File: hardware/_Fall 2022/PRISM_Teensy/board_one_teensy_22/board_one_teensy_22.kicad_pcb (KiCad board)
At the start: 2 copper layers, 0 parts

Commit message: Add GPS EAST
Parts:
- added C1: 0.1uf, Capacitor_SMD:C_0805_2012Metric_Pad1.18x1.45mm_HandSolder, F.Cu at (171.4, 62.9)
- added D1: LED, LED_SMD:LED_0805_2012Metric_Pad1.15x1.40mm_HandSolder, F.Cu at (145.7, 63.3)
- added D2: LED, LED_SMD:LED_0805_2012Metric_Pad1.15x1.40mm_HandSolder, F.Cu at (141.2, 63.3)
- added D3: LED, LED_SMD:LED_0805_2012Metric_Pad1.15x1.40mm_HandSolder, F.Cu at (136.8, 63.3)
- added J1: Conn_01x04, Connector_JST:JST_PH_S4B-PH-K_1x04_P2.00mm_Horizontal, F.Cu at (137.9, 63.5)
- added J2: Conn_01x07, Connector_JST:JST_PH_S7B-PH-K_1x07_P2.00mm_Horizontal, F.Cu at (123.8, 80.2)
- added R1: 150, Resistor_SMD:R_0805_2012Metric_Pad1.20x1.40mm_HandSolder, F.Cu at (145.7, 61.0)
- added R2: 150, Resistor_SMD:R_0805_2012Metric_Pad1.20x1.40mm_HandSolder, F.Cu at (141.2, 60.9)
- added R3: 150, Resistor_SMD:R_0805_2012Metric_Pad1.20x1.40mm_HandSolder, F.Cu at (136.8, 60.9)
- added R4: 100K, Resistor_SMD:R_0805_2012Metric_Pad1.20x1.40mm_HandSolder, F.Cu at (171.4, 72.3)
- added R5: 300K, Resistor_SMD:R_0805_2012Metric_Pad1.20x1.40mm_HandSolder, F.Cu at (171.4, 67.5)
- added U1: Teensy4.1, Teensy:Teensy41, F.Cu at (159.8, 92.6)
- added U2: BNO055_Breakout, Olin_Rocketry:BNO055, F.Cu at (134.6, 80.8)

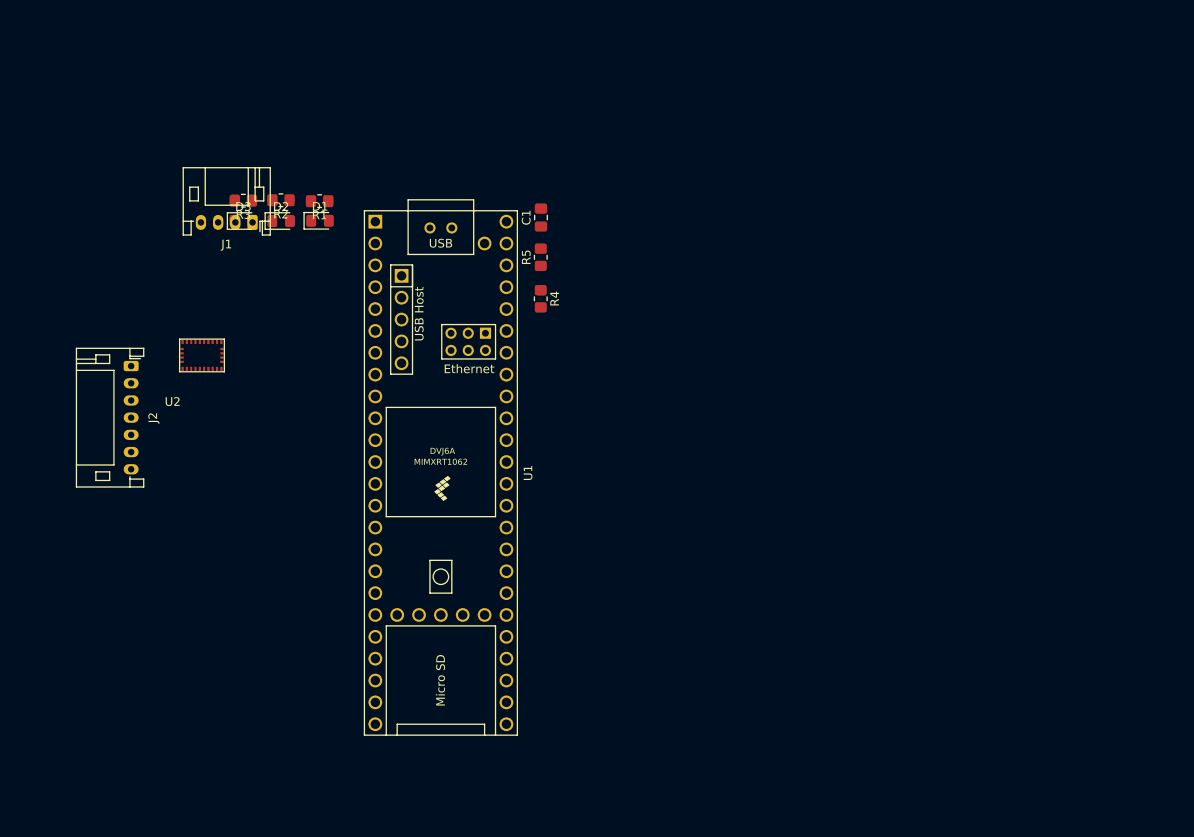
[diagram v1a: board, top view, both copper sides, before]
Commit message: reorganized PRISM FC
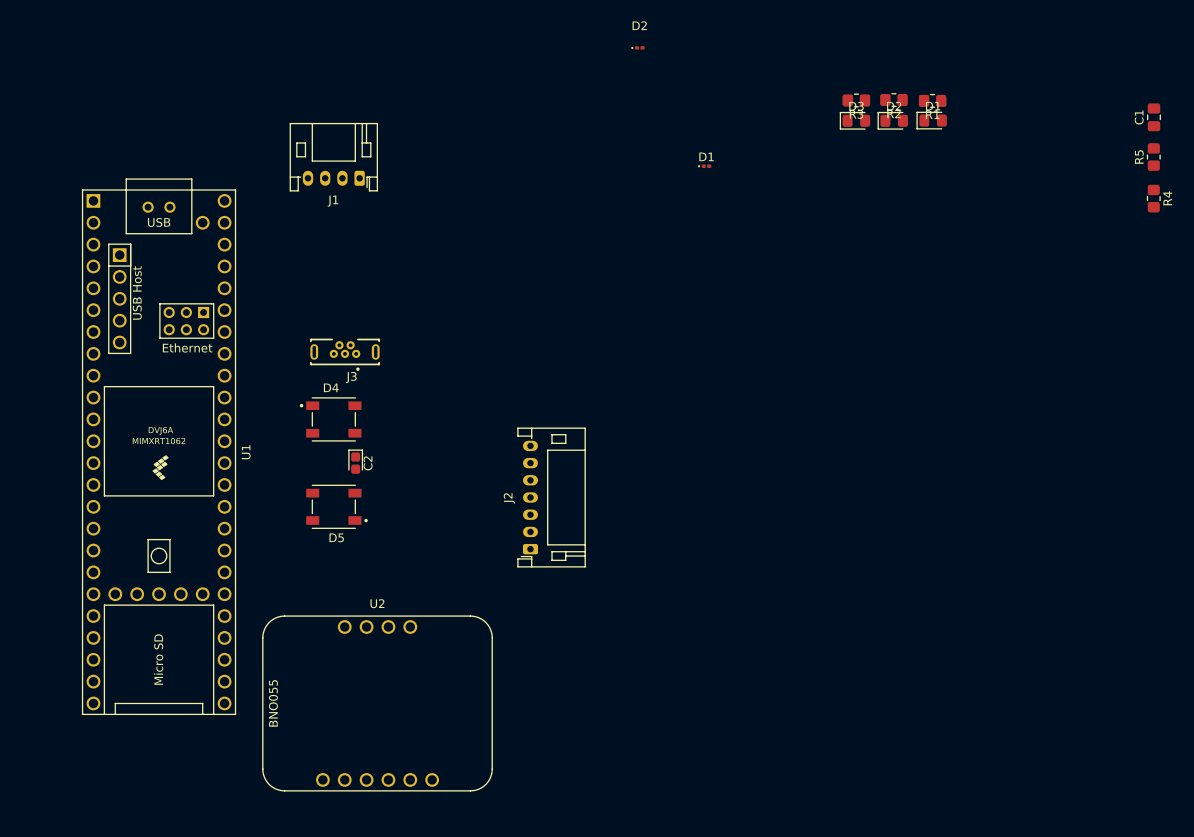
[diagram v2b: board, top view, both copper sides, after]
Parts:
- added C2: 0.1uf, Capacitor_Tantalum_SMD:CP_EIA-1608-08_AVX-J, F.Cu at (149.9, 91.4)
- added D1: DIODE, Diode_SMD:D_0201_0603Metric, F.Cu at (190.6, 56.9)
- added D2: DIODE, Diode_SMD:D_0201_0603Metric, F.Cu at (182.9, 43.2)
- added D4: Neopixel1, neopixel:LED_1655, F.Cu at (147.3, 86.4)
- added D5: Neopixel2, neopixel:LED_1655, F.Cu at (147.3, 96.5)
- added J3: USB_micro, USB:GCT_USB3131-30-0230-A_REVB, F.Cu at (148.6, 78.5)
- J1: value Conn_01x04 -> EAST
- J2: value Conn_01x07 -> CORE_IO
- U2: footprint Olin_Rocketry:BNO055 -> Sensors:BNO055_Breakout
- moved D1 72.2 mm to (217.0, 51.6)
- moved D3 72.2 mm to (208.1, 51.6)
- moved R3 72.2 mm to (208.1, 49.3)
- moved R4 72.2 mm to (242.6, 60.7)
- moved R5 72.2 mm to (242.6, 55.9)
- moved C1 72.2 mm to (242.7, 51.2)
- moved D2 72.2 mm to (212.5, 51.6)
- moved R1 72.2 mm to (216.9, 49.3)
- moved R2 72.2 mm to (212.4, 49.2)
- moved J2 51.1 mm to (170.2, 101.4), turned to 90 degrees
- moved U2 42.5 mm to (152.4, 119.4), turned to 0 degrees
- moved U1 32.9 mm to (127.0, 90.2)
- moved J1 13.5 mm to (150.3, 58.3)
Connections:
- R4 pad 1: /V_BATT -> /V_IN
- U1 pad 23: unconnected-(U1-Pad23) -> /NEOPIXEL
- U1 pad 48: /V_BATT -> /V_IN
- U1 pad 6: /LED 0 -> unconnected-(U1-Pad6)
- U1 pad 66: unconnected-(U1-Pad66) -> Net-(U1-Pad66)
- U1 pad 67: unconnected-(U1-Pad67) -> Net-(U1-Pad67)
- U1 pad 7: /LED 1 -> unconnected-(U1-Pad7)
- U1 pad 8: /LED 2 -> unconnected-(U1-Pad8)

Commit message: Add altimeter to footprint
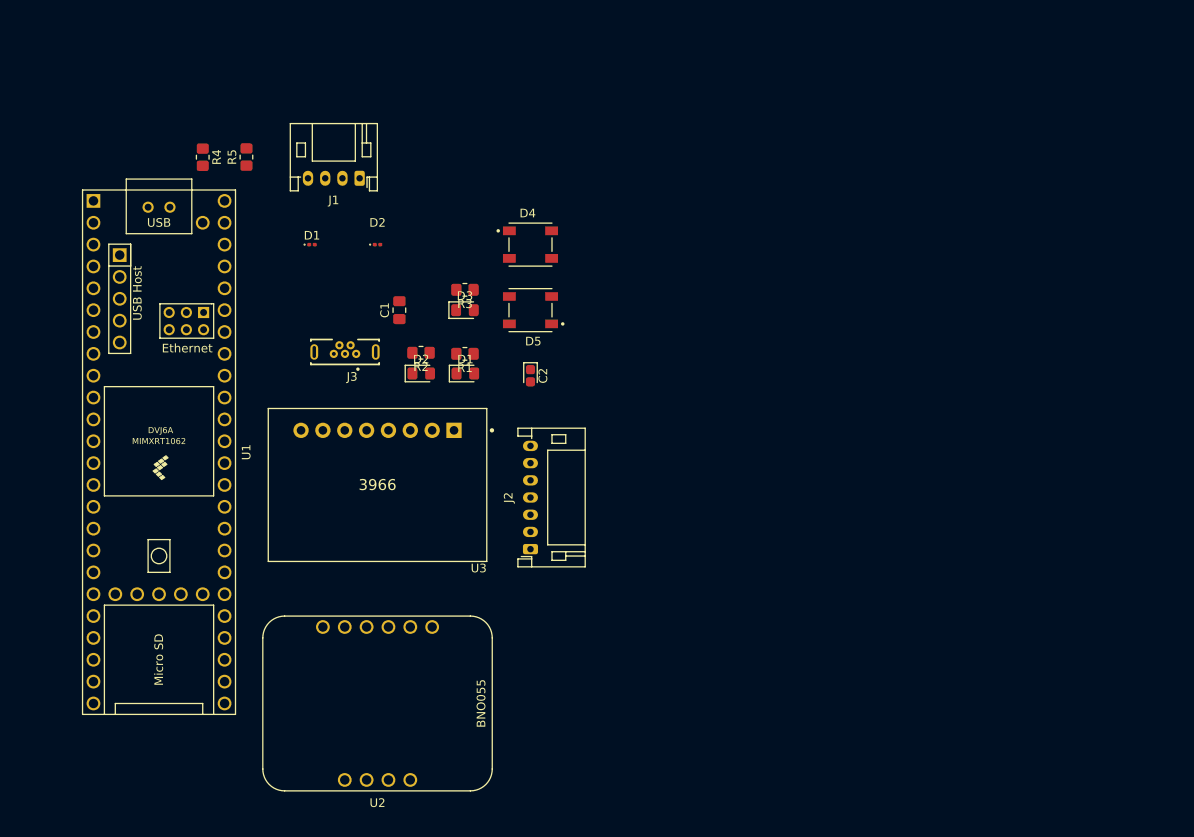
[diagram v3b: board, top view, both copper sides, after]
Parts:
- added U3: 3966, BMP388:Adafruit_Industries-3966-MFG, F.Cu at (152.4, 94.0)
- moved R4 110.7 mm to (132.1, 55.9)
- moved R5 105.5 mm to (137.2, 55.9)
- moved C1 90.5 mm to (154.9, 73.7)
- moved D2 62.3 mm to (157.5, 81.0)
- moved R2 62.3 mm to (157.5, 78.6)
- moved D1 61.8 mm to (162.6, 81.0)
- moved R1 61.8 mm to (162.6, 78.7)
- moved D3 50.5 mm to (162.6, 73.7)
- moved R3 50.5 mm to (162.6, 71.3)
- moved D1 46.8 mm to (144.8, 66.0)
- moved D2 38.1 mm to (152.4, 66.0)
- moved D5 32.3 mm to (170.2, 73.7)
- moved D4 30.6 mm to (170.2, 66.0)
- moved C2 22.7 mm to (170.2, 81.3)
- turned U2 to 180 degrees
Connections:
- J2 pad 1: GND -> /ARM
- J2 pad 2: /V_BATT -> /CONT 2
- J2 pad 3: /PYRO 1 -> /CONT 1
- J2 pad 5: /CONT 1 -> /PYRO 1
- J2 pad 6: /CONT 2 -> /VBAT
- J2 pad 7: /ARM -> GND

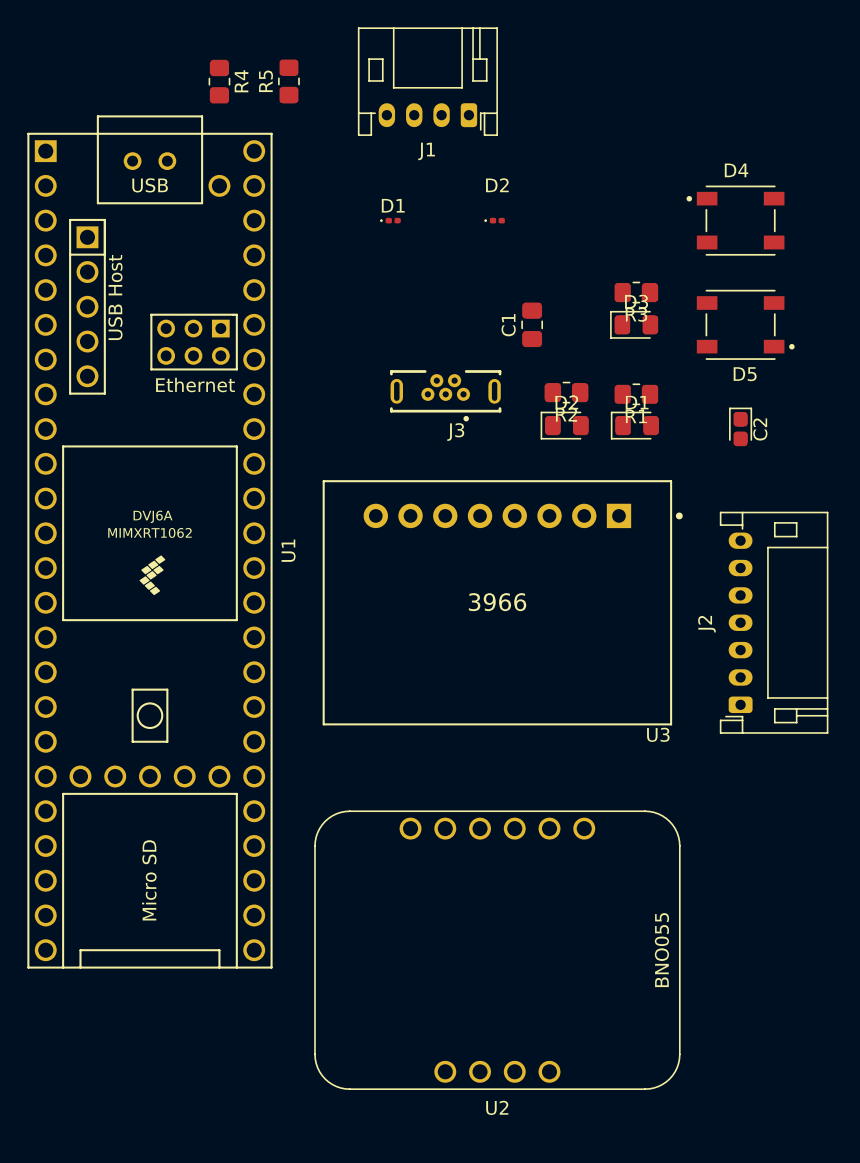
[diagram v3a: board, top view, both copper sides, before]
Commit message: Edit footprint layout and resistor sizes
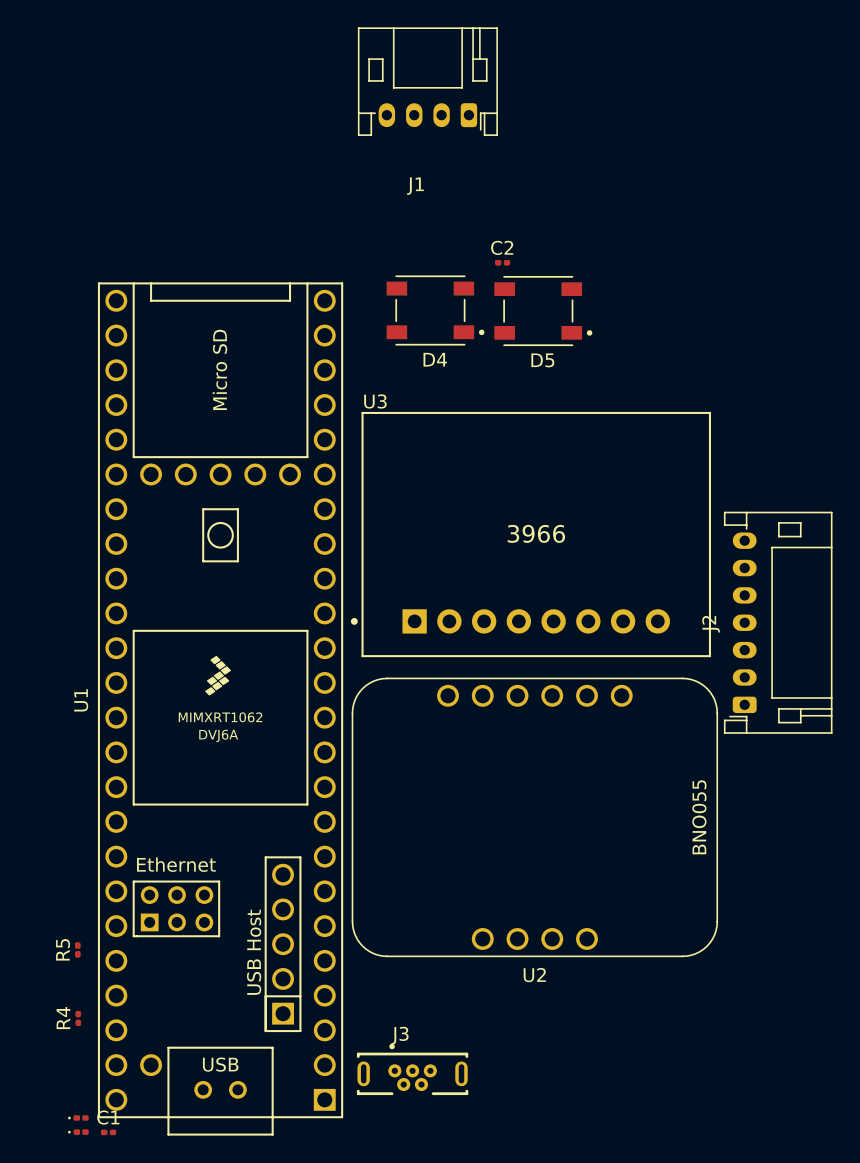
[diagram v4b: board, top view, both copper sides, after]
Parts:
- removed the D1 at (162.6, 81.0)
- removed the D2 at (157.5, 81.0)
- removed D3: LED, LED_SMD:LED_0805_2012Metric_Pad1.15x1.40mm_HandSolder
- removed R1, R2, R3: 150, Resistor_SMD:R_0805_2012Metric_Pad1.20x1.40mm_HandSolder
- C1: footprint Capacitor_SMD:C_0805_2012Metric_Pad1.18x1.45mm_HandSolder -> Capacitor_SMD:C_0201_0603Metric
- C2: footprint Capacitor_Tantalum_SMD:CP_EIA-1608-08_AVX-J -> Capacitor_SMD:C_0201_0603Metric
- R4, R5: footprint Resistor_SMD:R_0805_2012Metric_Pad1.20x1.40mm_HandSolder -> Resistor_SMD:R_0201_0603Metric
- moved D2 72.3 mm to (122.0, 131.7)
- moved D1 70.4 mm to (122.0, 132.7)
- moved R4 69.3 mm to (121.8, 124.4), turned to 90 degrees
- moved C1 66.7 mm to (124.0, 132.7), turned to 0 degrees
- moved R5 65.3 mm to (121.7, 119.4)
- moved J3 50.0 mm to (146.2, 128.4), turned to 0 degrees
- moved D4 23.6 mm to (147.5, 72.6), turned to 180 degrees
- moved C2 21.2 mm to (152.8, 69.1), turned to 0 degrees
- moved D5 14.8 mm to (155.4, 72.7)
- moved U1 12.1 mm to (132.2, 101.1), turned to 90 degrees
- moved U2 10.1 mm to (155.1, 109.7)
- moved U3 5.74 mm to (155.2, 89.0), turned to 0 degrees
- moved J2 0.30 mm to (170.5, 101.4)
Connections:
- R4 pad 1: /V_IN -> /VIN
- U1 pad 48: /V_IN -> /VIN

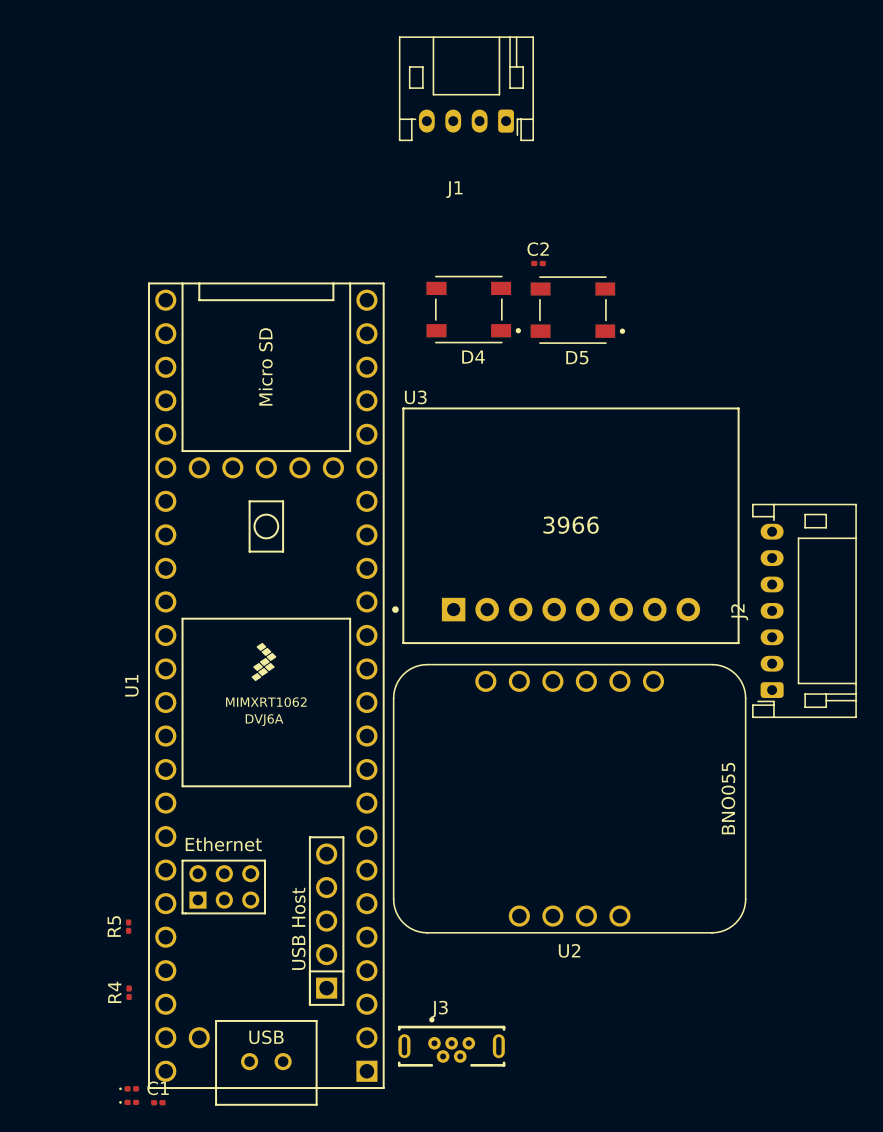
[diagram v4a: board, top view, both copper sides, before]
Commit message: Complete PRISM Teensy layout
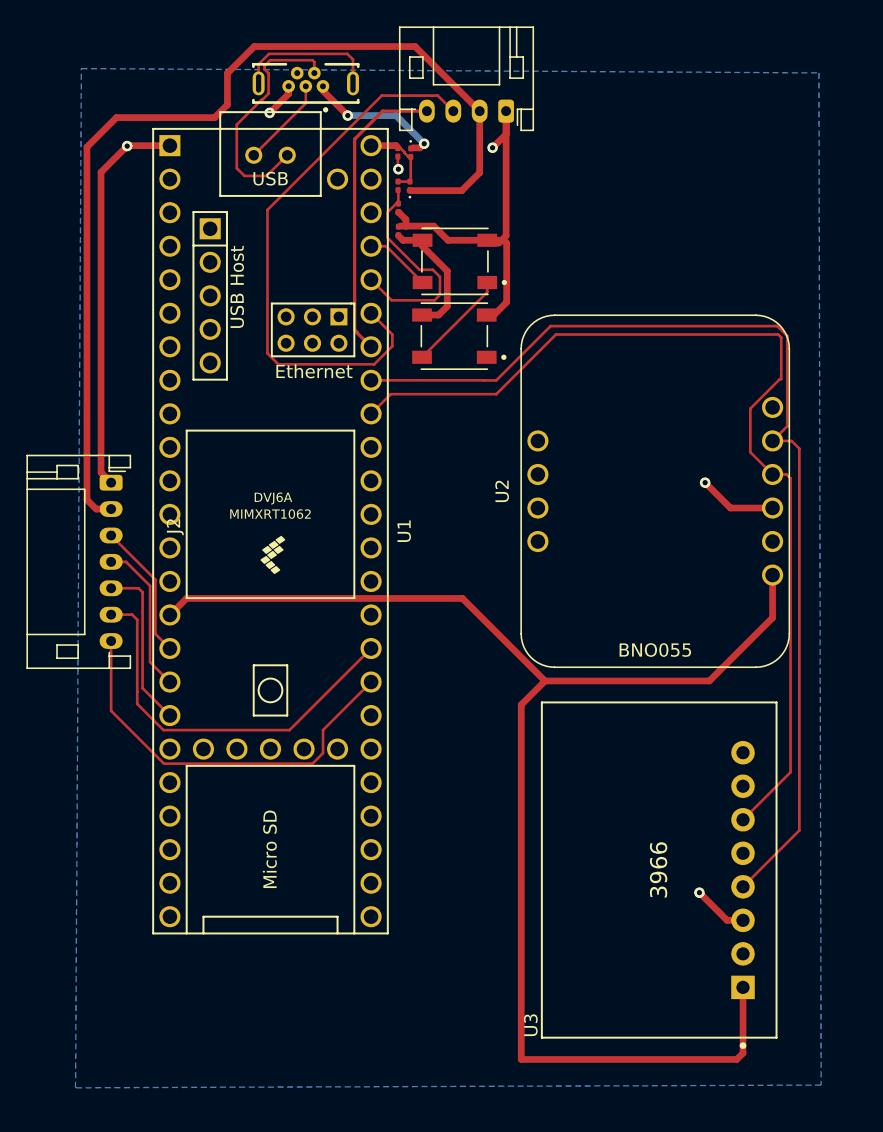
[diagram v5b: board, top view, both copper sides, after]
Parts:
- moved C1 74.3 mm to (142.1, 60.7), turned to -90 degrees
- moved D2 74.0 mm to (143.1, 60.7), turned to -90 degrees
- moved J3 73.8 mm to (135.2, 55.5), turned to 180 degrees
- moved D1 72.6 mm to (143.0, 63.2), turned to 90 degrees
- moved R4 64.4 mm to (142.1, 63.2), turned to -90 degrees
- moved R5 58.2 mm to (142.2, 64.9), turned to -90 degrees
- moved J2 52.5 mm to (120.4, 85.7), turned to -90 degrees
- moved U3 26.9 mm to (161.9, 115.1), turned to 90 degrees
- moved U2 24.2 mm to (161.6, 86.4), turned to 90 degrees
- moved U1 11.7 mm to (132.5, 89.4), turned to -90 degrees
- moved C2 10.9 mm to (142.2, 66.6), turned to -90 degrees
- moved D5 9.20 mm to (146.4, 74.6)
- moved D4 3.80 mm to (146.4, 69.0)
- moved J1 0.76 mm to (150.3, 57.6)
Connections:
- C1 pad 1: /V_BATT -> /VIN
- J1 pad 4: /RX 0  -> /RX 0
- J2 pad 1: /ARM -> GND
- J2 pad 2: /CONT 2 -> /V_BATT
- J2 pad 3: /CONT 1 -> /PYRO 1
- J2 pad 5: /PYRO 1 -> /ARM
- J2 pad 6: /VBAT -> /CONT 1
- J2 pad 7: GND -> /CONT 2
- J3 pad S1: Net-(J3-PadS1) -> unconnected-(J3-PadS1)
- J3 pad S2: Net-(J3-PadS1) -> unconnected-(J3-PadS1)
- U1 pad 10: /RX 0 -> unconnected-(U1-Pad10)
- U1 pad 23: /NEOPIXEL -> unconnected-(U1-Pad23)
- U1 pad 32: unconnected-(U1-Pad32) -> /CONT 2
- U1 pad 33: unconnected-(U1-Pad33) -> /CONT 1
- U1 pad 38: /CONT 2 -> unconnected-(U1-Pad38)
- U1 pad 39: /CONT 1 -> unconnected-(U1-Pad39)
- U1 pad 42: unconnected-(U1-Pad42) -> /RX 0
- U1 pad 43: unconnected-(U1-Pad43) -> /TX 0
- U1 pad 45: unconnected-(U1-Pad45) -> /NEOPIXEL
- U1 pad 9: /TX 0 -> unconnected-(U1-Pad9)
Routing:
- net /3.3V: track 0.00 -> 105.4 mm
- net /SCL 0: track 0.00 -> 79.2 mm
- net /V_BATT: track 0.00 -> 75.7 mm
- net /SDA 0: track 0.00 -> 74.6 mm
- net GND: track 0.00 -> 74.2 mm, vias 0 -> 6
- net /TX 0: track 0.00 -> 42.6 mm
- net /CONT 2: track 0.00 -> 30.2 mm
- net /CONT 1: track 0.00 -> 29.6 mm
- net /RX 0: track 0.00 -> 22.6 mm
- net Net-(J3-Pad2): track 0.00 -> 18.5 mm
- net Net-(R4-Pad2): track 0.00 -> 16.7 mm
- net /ARM: track 0.00 -> 12.7 mm
- net /PYRO 2: track 0.00 -> 11.6 mm
- net unconnected-(J3-PadS1): track 0.00 -> 10.9 mm
- net /V_USB: track 0.00 -> 10.7 mm, vias 0 -> 2
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- added copper zone on B.Cu, net GND
